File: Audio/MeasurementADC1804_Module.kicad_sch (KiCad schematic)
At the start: 78 parts, among them J701 Screw_Terminal_01x02, J702 Screw_Terminal_01x02, J703 Screw_Terminal_01x03, U701 OPA1656, U702 OPA1656, U703 OPA1656, U704 BP5293-50, U705 MBC2596-01, U706 LT1763-3.3, U707 LT1763-5, U708 TPS3808G33DBVR, U709 TPS3808G50DBVR, U710 XC8107AC20MR-G, Y701 ASFL1-12.288MHZ-EC-T

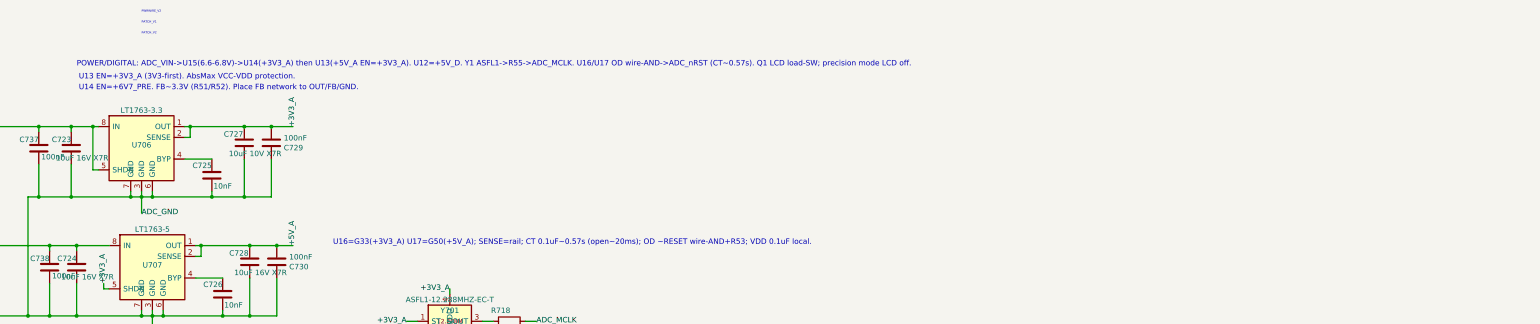
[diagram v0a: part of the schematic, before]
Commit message: レビュー指摘の任意項目を直し、旧注記と未使用AO3401定義を片付ける。
POWER/DIGITAL注記をU704–U710表記に揃え、CT open≈20msに修正。初号はLCD常時ON可と明記する。

Co-authored-by: Cursor <cursoragent@cursor.com>
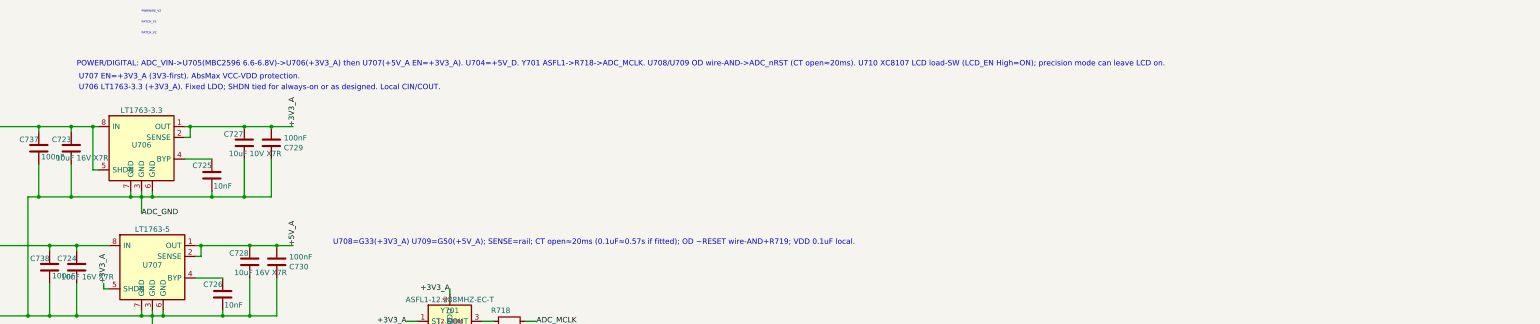
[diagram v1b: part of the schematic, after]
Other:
- note added: "POWER/DIGITAL: ADC_VIN->U705(MBC2596 6.6-6.8V)->U706(+3V3_A) then U707(+5V_A EN=+3V3_A). U704=+5V_D. Y701 ASFL1->R718->ADC_MCLK. U708/U709 OD wire-AND->ADC_nRST (CT open≈20ms). U710 XC8107 LCD load-SW (LCD_EN High=ON); precision mode can leave LCD on."
- note added: "U706 LT1763-3.3 (+3V3_A). Fixed LDO; SHDN tied for always-on or as designed. Local CIN/COUT."
- note added: "U707 EN=+3V3_A (3V3-first). AbsMax VCC-VDD protection."
- note added: "U708=G33(+3V3_A) U709=G50(+5V_A); SENSE=rail; CT open≈20ms (0.1uF≈0.57s if fitted); OD ~RESET wire-AND+R719; VDD 0.1uF local."
- note removed: "POWER/DIGITAL: ADC_VIN->U15(6.6-6.8V)->U14(+3V3_A) then U13(+5V_A EN=+3V3_A). U12=+5V_D. Y1 ASFL1->R55->ADC_MCLK. U16/U17 OD wire-AND->ADC_nRST (CT~0.57s). Q1 LCD load-SW; precision mode LCD off."
- note removed: "U13 EN=+3V3_A (3V3-first). AbsMax VCC-VDD protection."
- note removed: "U14 EN=+6V7_PRE. FB~3.3V (R51/R52). Place FB network to OUT/FB/GND."
- note removed: "U16=G33(+3V3_A) U17=G50(+5V_A); SENSE=rail; CT 0.1uF~0.57s (open~20ms); OD ~RESET wire-AND+R53; VDD 0.1uF local."

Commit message: U710注記を初号LCD常時ON可に合わせて更新する。
Co-authored-by: Cursor <cursoragent@cursor.com>
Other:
- note added: "U710 XC8107AC20MR-G ロードスイッチ: LCD_EN High=ON / Low・Hi-Z=OFF（Active High, VCEH 1.5V min → Pico 3.3V で直接駆動可）。R717 100k=CE プルダウンで起動時 OFF。初号は常時 ON 可。OFF 運用時は SPI/タッチを Low/Hi-Z に。ソフトスタート 0.6ms typ・短絡/逆流/過熱/UVLO 保護内蔵。C740=CIN, C739=CL は各 10uF/3216 を IC 直近へ。FLG は未使用（NC）。"
- note removed: "U710 XC8107AC20MR-G ロードスイッチ: LCD_EN High=ON / Low・Hi-Z=OFF（Active High, VCEH 1.5V min → Pico 3.3V で直接駆動可）。R717 100k=CE プルダウンで起動時 OFF。ノイズ床測定は LCD_EN=Low のまま。ソフトスタート 0.6ms typ・短絡/逆流/過熱/UVLO 保護内蔵。C740=CIN, C739=CL は各 10uF/3216 を IC 直近へ（推奨 1uF 以上）。FLG は未使用（NC）。"
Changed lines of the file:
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@@
 		)
 	)
-	(text "U710 XC8107AC20MR-G ロードスイッチ: LCD_EN High=ON / Low・Hi-Z=OFF（Active High, VCEH 1.5V min → Pico 3.3V で直接駆動可）。R717 100k=CE プルダウンで起動時 OFF。ノイズ床測定は LCD_EN=Low のまま。ソフトスタート 0.6ms typ・短絡/逆流/過熱/UVLO 保護内蔵。C740=CIN, C739=CL は各 10uF/3216 を IC 直近へ（推奨 1uF 以上）。FLG は未使用（NC）。"
+	(text "U710 XC8107AC20MR-G ロードスイッチ: LCD_EN High=ON / Low・Hi-Z=OFF（Active High, VCEH 1.5V min → Pico 3.3V で直接駆動可）。R717 100k=CE プルダウンで起動時 OFF。初号は常時 ON 可。OFF 運用時は SPI/タッチを Low/Hi-Z に。ソフトスタート 0.6ms typ・短絡/逆流/過熱/UVLO 保護内蔵。C740=CIN, C739=CL は各 10uF/3216 を IC 直近へ。FLG は未使用（NC）。"
 		(exclude_from_sim no)
 		(at 312.42 163.83 0)

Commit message: MeasurementADCの配置準備とMBC2596向き修正、KiCad MCP設定を追加する。
C739/C740を購入済み3216に合わせ、ゾーン仮配置とREADMEのポータブルMCP手順を残す。

Co-authored-by: Cursor <cursoragent@cursor.com>
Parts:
- C739: renamed from C733; value 100nF -> 10uF 50V X7R; footprint Capacitor_THT:C_Disc_D5.0mm_W2.5mm_P5.00mm -> Capacitor_SMD:C_1206_3216Metric_Pad1.33x1.80mm_HandSolder
- C740: renamed from C734; value 100nF -> 10uF 50V X7R; footprint Capacitor_THT:C_Disc_D5.0mm_W2.5mm_P5.00mm -> Capacitor_SMD:C_1206_3216Metric_Pad1.33x1.80mm_HandSolder
- J701: value Screw_Terminal_01x02 -> AUDIO
- J702: value Screw_Terminal_01x02 -> V_IN
- J703: value Screw_Terminal_01x03 -> 15_V_IN
- renumbered C712 to C711, C713 to C712, C717 to C713, C718 to C714, C719 to C715, C720 to C716, C721 to C717, C722 to C718, C711 to C719, C715 to C720, C714 to C721, C716 to C722, C740 to C723, C737 to C724, C738 to C725, C723 to C726, C724 to C727, C736 to C728, C735 to C729, C725 to C730, C726 to C731, C727 to C732, C728 to C733, C739 to C734, C729 to C735, C730 to C736, C731 to C737, C732 to C738, U710 to U708, U708 to U709, U709 to U710

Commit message: ムラタRDEのフットプリントを実寸に合わせ、STATUSを現状に更新する。
Disc φ5汎用FPが過大で干渉誤認の原因だったため、発注品RDER71Hに合わせたFPへ20箇所を差し替える。

Co-authored-by: Cursor <cursoragent@cursor.com>
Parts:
- C701, C702, C705, C706, C711, C712, C717, C718, C719, C720, C722, C724, C725, C728, C730, C731, C735, C736, C737, C738: footprint Capacitor_THT:C_Disc_D5.0mm_W2.5mm_P5.00mm -> Library:C_Murata_RDE_L4.0mm_W3.5mm_T2.5mm_P5.00mm
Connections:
- net +15V_A: now also J703.3 (Pin_3); no longer J703.1 (Pin_1)
- net -15V_A: now also J703.1 (Pin_1); no longer J703.3 (Pin_3)
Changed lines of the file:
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@@
 		)
 	)
+	(label "-15V_A"
+		(at 111.76 227.33 0)
+		(effects
+			(font
+				(size 1.27 1.27)
+			)
+			(justify left bottom)
+		)
+	)
 	(label "AUDIO_L_IN"
 		(at 33.02 26.67 180)
@@
 		)
 	)
-	(label "-15V_A"
-		(at 101.6 227.33 180)
+	(label "TP_SDA"
+		(at 247.65 177.8 180)
 		(effects
 			(font
 				(size 1.27 1.27)
 			)
-			(justify right bottom)
+			(justify right)
 		)
 	)
-	(label "TP_SDA"
-		(at 247.65 177.8 180)
+	(label "+15V_A"
+		(at 101.6 227.33 180)
 		(effects
 			(font
 				(size 1.27 1.27)
 			)
-			(justify right)
+			(justify right bottom)
 		)
 	)
@@
 		)
 	)
-	(label "+15V_A"
-		(at 111.76 227.33 0)
-		(effects
-			(font
-				(size 1.27 1.27)
-			)
-			(justify left bottom)
-		)
-	)
 	(label "LCD_CS"
 		(at 194.31 171.45 180)
@@
 		)
 	)
-	(hierarchical_label "-15V_A"
-		(shape input)
-		(at 102.87 223.52 180)
+	(hierarchical_label "A_GND"
+		(shape bidirectional)
+		(at 105.41 215.9 180)
 		(effects
 			(font
@@
 		)
 	)
-	(hierarchical_label "A_GND"
-		(shape bidirectional)
-		(at 105.41 215.9 180)
+	(hierarchical_label "ADC_GND_IN"
+		(shape input)
+		(at 66.04 219.71 0)
 		(effects
 			(font
 				(size 1.524 1.524)
 			)
-			(justify right)
+			(justify left)
 		)
 	)
-	(hierarchical_label "+15V_A"
+	(hierarchical_label "ADC_V_IN"
 		(shape input)
-		(at 110.49 223.52 0)
+		(at 63.5 219.71 180)
 		(effects
 			(font
 				(size 1.524 1.524)
 			)
-			(justify left)
+			(justify right)
 		)
 	)
-	(hierarchical_label "ADC_GND_IN"
+	(hierarchical_label "-15V_A"
 		(shape input)
-		(at 66.04 219.71 0)
+		(at 110.49 223.52 0)
 		(effects
 			(font
@@
 		)
 	)
-	(hierarchical_label "ADC_V_IN"
+	(hierarchical_label "AUDIO_R_IN"
 		(shape input)
-		(at 63.5 219.71 180)
+		(at 22.86 219.71 180)
 		(effects
 			(font
@@
 		)
 	)
-	(hierarchical_label "AUDIO_R_IN"
+	(hierarchical_label "+15V_A"
 		(shape input)
-		(at 22.86 219.71 180)
+		(at 102.87 223.52 180)
 		(effects
 			(font
@@
 			)
 		)
-		(property "Footprint" "Capacitor_THT:C_Disc_D5.0mm_W2.5mm_P5.00mm"
+		(property "Footprint" "Library:C_Murata_RDE_L4.0mm_W3.5mm_T2.5mm_P5.00mm"
 			(at 34.29 196.85 0)
 			(hide yes)
@@
 			)
 		)
-		(property "Footprint" "Capacitor_THT:C_Disc_D5.0mm_W2.5mm_P5.00mm"
+		(property "Footprint" "Library:C_Murata_RDE_L4.0mm_W3.5mm_T2.5mm_P5.00mm"
 			(at 316.23 36.83 0)
 			(hide yes)
@@
 			)
 		)
-		(property "Footprint" "Capacitor_THT:C_Disc_D5.0mm_W2.5mm_P5.00mm"
+		(property "Footprint" "Library:C_Murata_RDE_L4.0mm_W3.5mm_T2.5mm_P5.00mm"
 			(at 370.84 35.56 0)
 			(hide yes)
@@
 			)
 		)
-		(property "Footprint" "Capacitor_THT:C_Disc_D5.0mm_W2.5mm_P5.00mm"
+		(property "Footprint" "Library:C_Murata_RDE_L4.0mm_W3.5mm_T2.5mm_P5.00mm"
 			(at 72.39 196.85 0)
 			(hide yes)
@@
 			)
 		)
-		(property "Footprint" "Capacitor_THT:C_Disc_D5.0mm_W2.5mm_P5.00mm"
+		(property "Footprint" "Library:C_Murata_RDE_L4.0mm_W3.5mm_T2.5mm_P5.00mm"
 			(at 359.41 71.12 0)
 			(hide yes)
@@
 			)
 		)
-		(property "Footprint" "Capacitor_THT:C_Disc_D5.0mm_W2.5mm_P5.00mm"
+		(property "Footprint" "Library:C_Murata_RDE_L4.0mm_W3.5mm_T2.5mm_P5.00mm"
 			(at 104.14 196.85 0)
 			(hide yes)
@@
 			)
 		)
-		(property "Footprint" "Capacitor_THT:C_Disc_D5.0mm_W2.5mm_P5.00mm"
+		(property "Footprint" "Library:C_Murata_RDE_L4.0mm_W3.5mm_T2.5mm_P5.00mm"
 			(at 330.2 130.81 0)
 			(hide yes)
@@
 			)
 		)
-		(property "Footprint" "Capacitor_THT:C_Disc_D5.0mm_W2.5mm_P5.00mm"
+		(property "Footprint" "Library:C_Murata_RDE_L4.0mm_W3.5mm_T2.5mm_P5.00mm"
 			(at 398.78 134.62 0)
 			(hide yes)
@@
 			)
 		)
-		(property "Footprint" "Capacitor_THT:C_Disc_D5.0mm_W2.5mm_P5.00mm"
+		(property "Footprint" "Library:C_Murata_RDE_L4.0mm_W3.5mm_T2.5mm_P5.00mm"
 			(at 152.4 41.91 0)
 			(hide yes)
@@
 			)
 		)
-		(property "Footprint" "Capacitor_THT:C_Disc_D5.0mm_W2.5mm_P5.00mm"
+		(property "Footprint" "Library:C_Murata_RDE_L4.0mm_W3.5mm_T2.5mm_P5.00mm"
 			(at 356.87 43.18 0)
 			(hide yes)
@@
 			)
 		)
-		(property "Footprint" "Capacitor_THT:C_Disc_D5.0mm_W2.5mm_P5.00mm"
+		(property "Footprint" "Library:C_Murata_RDE_L4.0mm_W3.5mm_T2.5mm_P5.00mm"
 			(at 152.4 62.23 0)
 			(hide yes)
@@
 			)
 		)
-		(property "Footprint" "Capacitor_THT:C_Disc_D5.0mm_W2.5mm_P5.00mm"
+		(property "Footprint" "Library:C_Murata_RDE_L4.0mm_W3.5mm_T2.5mm_P5.00mm"
 			(at 34.29 189.23 0)
 			(hide yes)
@@
 			)
 		)
-		(property "Footprint" "Capacitor_THT:C_Disc_D5.0mm_W2.5mm_P5.00mm"
+		(property "Footprint" "Library:C_Murata_RDE_L4.0mm_W3.5mm_T2.5mm_P5.00mm"
 			(at 135.89 196.85 0)
 			(hide yes)
@@
 			)
 		)
-		(property "Footprint" "Capacitor_THT:C_Disc_D5.0mm_W2.5mm_P5.00mm"
+		(property "Footprint" "Library:C_Murata_RDE_L4.0mm_W3.5mm_T2.5mm_P5.00mm"
 			(at 104.14 189.23 0)
 			(hide yes)
@@
 			)
 		)
-		(property "Footprint" "Capacitor_THT:C_Disc_D5.0mm_W2.5mm_P5.00mm"
+		(property "Footprint" "Library:C_Murata_RDE_L4.0mm_W3.5mm_T2.5mm_P5.00mm"
 			(at 398.78 104.14 0)
 			(hide yes)
@@
 			)
 		)
-		(property "Footprint" "Capacitor_THT:C_Disc_D5.0mm_W2.5mm_P5.00mm"
+		(property "Footprint" "Library:C_Murata_RDE_L4.0mm_W3.5mm_T2.5mm_P5.00mm"
 			(at 135.89 189.23 0)
 			(hide yes)
@@
 			)
 		)
-		(property "Footprint" "Capacitor_THT:C_Disc_D5.0mm_W2.5mm_P5.00mm"
+		(property "Footprint" "Library:C_Murata_RDE_L4.0mm_W3.5mm_T2.5mm_P5.00mm"
 			(at 372.11 63.5 0)
 			(hide yes)
@@
 			)
 		)
-		(property "Footprint" "Capacitor_THT:C_Disc_D5.0mm_W2.5mm_P5.00mm"
+		(property "Footprint" "Library:C_Murata_RDE_L4.0mm_W3.5mm_T2.5mm_P5.00mm"
 			(at 288.29 46.99 0)
 			(hide yes)
@@
 			)
 		)
-		(property "Footprint" "Capacitor_THT:C_Disc_D5.0mm_W2.5mm_P5.00mm"
+		(property "Footprint" "Library:C_Murata_RDE_L4.0mm_W3.5mm_T2.5mm_P5.00mm"
 			(at 72.39 189.23 0)
 			(hide yes)
@@
 			)
 		)
-		(property "Footprint" "Capacitor_THT:C_Disc_D5.0mm_W2.5mm_P5.00mm"
+		(property "Footprint" "Library:C_Murata_RDE_L4.0mm_W3.5mm_T2.5mm_P5.00mm"
 			(at 318.77 64.77 0)
 			(hide yes)

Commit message: 電源島の配置配線を進め、STATUSに次タスクを残す。
CIN(C741/C742)と+5V_D幹線・U705寄せ・NT702周りを反映し、引き継ぎ用の優先作業を STATUS 先頭にメモした。

Co-authored-by: Cursor <cursoragent@cursor.com>
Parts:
- added C741: 47uF 35V, Capacitor_THT:CP_Radial_D8.0mm_P3.50mm, symbol Device:C_Polarized
- added C742: 100nF, Library:C_Murata_RDE_L4.0mm_W3.5mm_T2.5mm_P5.00mm, symbol Device:C
- added F701: Fuse, symbol Device:Fuse
- A702: footprint Module:RaspberryPi_Pico_Common_Unspecified -> Module:RaspberryPi_Pico_Common_THT
- C705, C706, C711, C712, C717, C718: footprint Library:C_Murata_RDE_L4.0mm_W3.5mm_T2.5mm_P5.00mm -> Capacitor_SMD:C_1206_3216Metric_Pad1.33x1.80mm_HandSolder
- NT701, NT702: footprint NetTie:NetTie-2_THT_Pad1.0mm -> NetTie:NetTie-2_SMD_Pad2.0mm
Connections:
- net ADC_GND_IN: now also J702.2 (Pin_2), C741.2, C742.2; no longer J702.1 (Pin_1)
- net ADC_V_IN: now also C741.1, C742.1, F701.2; no longer J702.2 (Pin_2)
- net AUDIO_L_IN: now also C708.2, J701.2 (Pin_2), R701.2; no longer C710.2, J701.1 (Pin_1), R702.2
- net AUDIO_R_IN: now also C710.2, J701.1 (Pin_1), R702.2; no longer C708.2, J701.2 (Pin_2), R701.2
- net VCOML: now also C720.2, U703.3 (INA+), U703.5 (INB+); no longer C719.2, U702.3 (INA+), U702.5 (INB+)
- net VCOMR: now also C719.2, U702.3 (INA+), U702.5 (INB+); no longer C720.2, U703.3 (INA+), U703.5 (INB+)
- net VINL+: now also R716.1; no longer R714.1
- net VINL-: now also R715.1; no longer R713.1
- net VINR+: now also R714.1; no longer R716.1
- net VINR-: now also R713.1; no longer R715.1
- new net: F701.1, J702.1 (Pin_1)
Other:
- note added: "左チャンネル"
- note added: "階層ポート / 右チャンネル"
- note removed: "右チャンネル"
- note removed: "階層ポート / 左チャンネル"

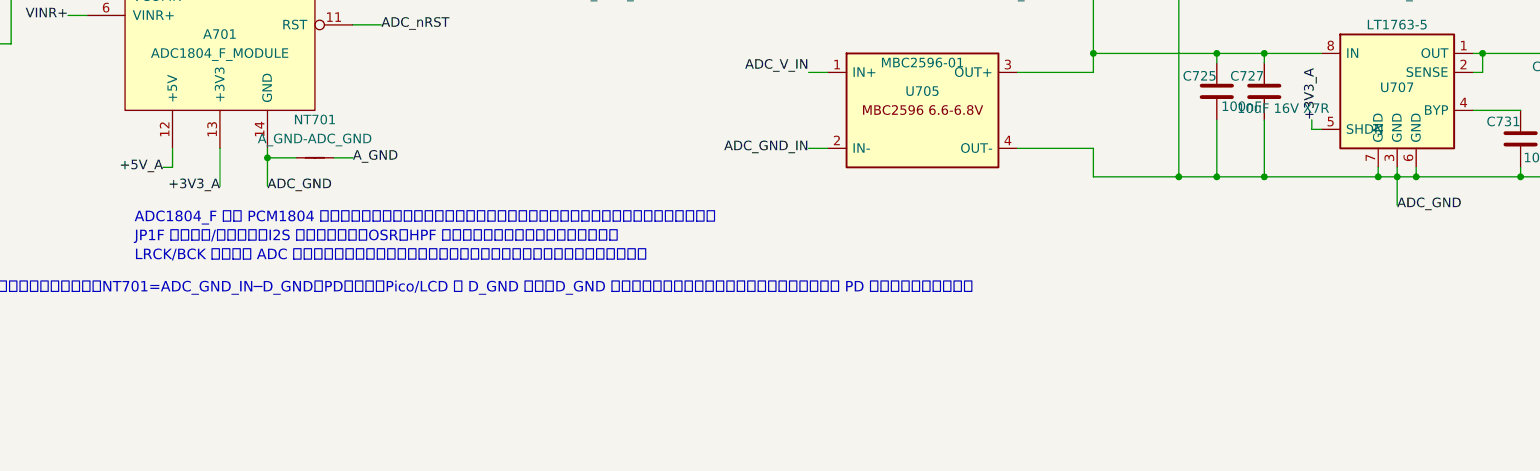
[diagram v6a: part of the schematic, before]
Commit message: 計測ADC周りのDRC・方針整理とGNDベタ直角化を反映する。
A702嵩上げコートヤード緩和、A701固定穴ノッチ、F701/FMT注記、LCDソフト制御とSTATUS更新をまとめる。

Co-authored-by: Cursor <cursoragent@cursor.com>
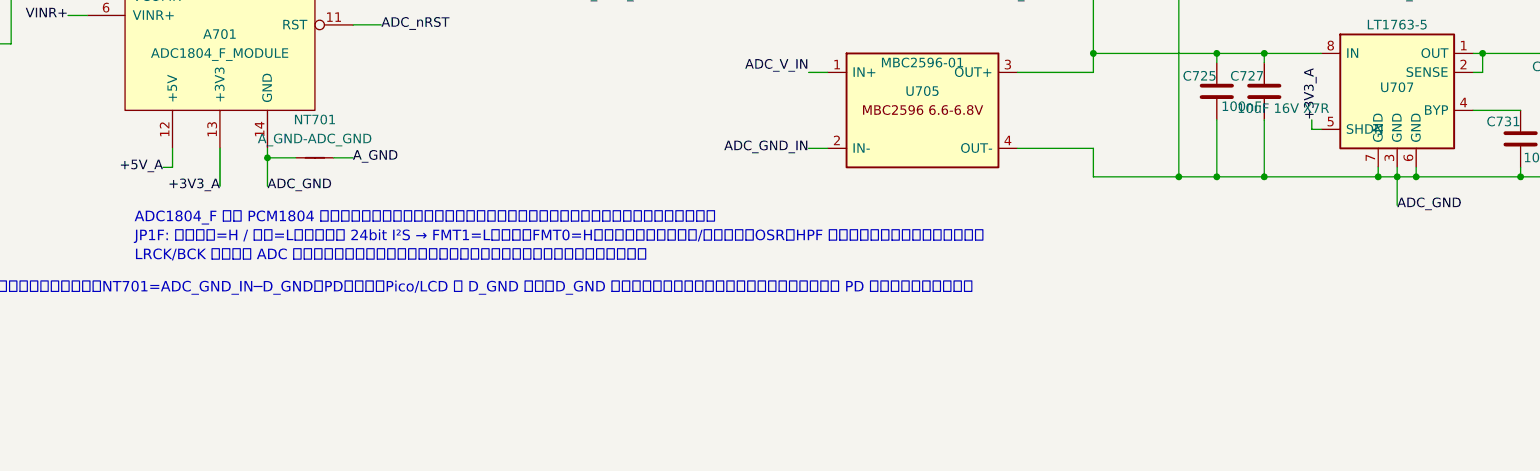
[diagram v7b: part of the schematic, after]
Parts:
- F701: footprint (none) -> Resistor_THT:R_Axial_DIN0411_L9.9mm_D3.6mm_P12.70mm_Horizontal
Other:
- note added: "JP1F: ショート=H / 開放=L。本設計は 24bit I²S → FMT1=L（開放）FMT0=H（ショート）。マスタ/スレーブ・OSR・HPF はモジュールマニュアルに従う。"
- note removed: "JP1F でマスタ/スレーブ、I2S フォーマット、OSR、HPF をモジュールマニュアルに従い設定。"
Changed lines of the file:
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@@
 		)
 	)
-	(text "JP1F でマスタ/スレーブ、I2S フォーマット、OSR、HPF をモジュールマニュアルに従い設定。"
+	(text "JP1F: ショート=H / 開放=L。本設計は 24bit I²S → FMT1=L（開放）FMT0=H（ショート）。マスタ/スレーブ・OSR・HPF はモジュールマニュアルに従う。"
 		(exclude_from_sim no)
 		(at 173.99 85.09 0)
@@
 			)
 		)
-		(property "Footprint" ""
+		(property "Footprint" "Resistor_THT:R_Axial_DIN0411_L9.9mm_D3.6mm_P12.70mm_Horizontal"
 			(at 67.818 223.52 90)
 			(hide yes)

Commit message: 計測ADC回路図を rev 0.4 として固定し、監視ICを TPS3307 に置き換える。
初号の応急配線（LCD SPI0、D701、GP15=~MR）を正規化し、U709 VDD 短絡も直した。ネット照合用スクリプトも残す。

Co-authored-by: Cursor <cursoragent@cursor.com>
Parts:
- removed C739: 10uF 50V X7R, Capacitor_SMD:C_1206_3216Metric_Pad1.33x1.80mm_HandSolder, symbol Device:C
- removed U709: TPS3808G33DBVR, Package_TO_SOT_SMD:SOT-23-6, symbol MeasurementADC_Extras:TPS3808G33DBVR
- removed U710: TPS3808G50DBVR, Package_TO_SOT_SMD:SOT-23-6, symbol MeasurementADC_Extras:TPS3808G50DBVR
- added C743: 100nF, Capacitor_SMD:C_0603_1608Metric, symbol Device:C
- added C744: 10nF, Capacitor_SMD:C_0603_1608Metric, symbol Device:C
- added D701: RB160M-30, Diode_SMD:D_SOD-123, symbol Device:D_Schottky
- added R720: 1k, Resistor_SMD:R_1206_3216Metric_Pad1.30x1.75mm_HandSolder, symbol Device:R
- added TP701: ADC_MCLK, TestPoint:TestPoint_Pad_D1.5mm, symbol Connector:TestPoint
- added U709: TPS3307-33D, Package_SO:SOIC-8_3.9x4.9mm_P1.27mm, symbol MeasurementADC_Extras:TPS3307-33
- C737: value 10nF -> 100nF; footprint Library:C_Murata_RDE_L4.0mm_W3.5mm_T2.5mm_P5.00mm -> Capacitor_SMD:C_0603_1608Metric
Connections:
- net +3V3_A: now also C743.1, C744.1, U709.2 (SENSE2), U709.3 (SENSE3), U709.8 (VDD); no longer C737.2
- net +5V_A: now also C737.2, U709.1 (SENSE1)
- net +5V_D: now also D701.2 (A); no longer A702.39 (VSYS)
- net ADC_GND: now also C743.2, C744.2, U709.4 (GND)
- net ADC_MCLK: now also R720.1, TP701.1
- net ADC_nRST: now also U709.5 (~{RESET})
- net LCD_MOSI: now also A702.25 (GPIO19); no longer A702.6 (GPIO4)
- net LCD_SCK: now also A702.24 (GPIO18); no longer A702.5 (GPIO3)
- net MCLK_SENSE: now reaches A702.12 (GPIO9)
- net MCLK_SENSE: now also R720.2
- net ADC_nMR: now reaches A702.20 (GPIO15)
- net ADC_nMR: now also U709.7 (~{MR})
- new net VSYS: A702.39 (VSYS), D701.1 (K)
- no-connect marks 22 -> 18
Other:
- note added: "A3 Pico2 横置き: 南列 1-20 西→東 / 北列 21-40 東→西。VSYS=+5V_D via D701 ショットキ, GND=D_GND | GP0=ADC_DATA GP1=ADC_BCK GP2=ADC_LRCK | GP3/GP4=NC(旧 LCD SPI) | GP5=LCD_CS GP6=LCD_DC GP7=LCD_RST GP8=LCD_EN | GP9=MCLK_SENSE (R720 1k, 入力専用) | GP10=TP_SDA GP11=TP_SCL GP12=TP_INT GP13=TP_RST | GP15=ADC_nMR (TPS3307 ~MR, OD, H は駆動しない) | GP18=LCD_SCK GP19=LCD_MOSI (SPI0)"
- note added: "GP15=ADC_nMR は TPS3307 の ~MR。オープンドレインのみ、H は駆動しない。 ~RESET はプッシュプルなので ADC_nRST には直接ワイヤ AND しない。"
- note added: "GP9=MCLK_SENSE は R720 1k 経由の入力専用。出力にすると Y701 と衝突して SCKI が化ける。"
- note added: "JP1F: ショート=H / 開放=L。本設計は S/M=L, OSR2=L OSR1=H OSR0=H（ADCマスタ 48k/256fs）、24bit I²S → FMT1=L（開放）FMT0=H（ショート）。HPF はモジュールマニュアルに従う。"
- note added: "POWER/DIGITAL: ADC_VIN->U705(MBC2596 6.6-6.8V)->U706(+3V3_A) then U707(+5V_A EN=+3V3_A). U704=+5V_D; D701 Schottky +5V_D->VSYS so USB cannot backfeed +5V_D. Y701 ASFL1->R718->ADC_MCLK (TP701; R720 1k to GP9 sense). U709 TPS3307-33D SO-8 watches +5V_A/+3V3_A, ~RESET->ADC_nRST (PP, 200ms), GP15 OD -> ~MR. U708 XC8107 LCD load-SW (LCD_EN High=ON)."
- note added: "U708 XC8107AC20MR-G ロードスイッチ: LCD_EN High=ON / Low・Hi-Z=OFF（Active High, VCEH 1.5V min → Pico 3.3V で直接駆動可）。R717 100k=CE プルダウンで起動時 OFF。初号は常時 ON 可。OFF 運用時は SPI/タッチを Low/Hi-Z に。ソフトスタート 0.6ms typ・短絡/逆流/過熱/UVLO 保護内蔵。C740=CIN, C739=CL は各 10uF/3216 を IC 直近へ。FLG は未使用（NC）。"
- note added: "U709=TPS3307-33D SO-8: SENSE1=+5V_A (4.55V) SENSE2=+3V3_A (2.93V) SENSE3=VDD; VDD=+3V3_A C745 100nF; ~RESET PP -> ADC_nRST + R719; GP15 OD -> ~MR (do not drive H); RESET pin NC; 200ms delay. Replaces TPS3808G33/G50 SOT-23-6."
- note added: "電源: USB VBUS → Pico 内部ショットキ → VSYS。D701 が +5V_D への逆流を止めるので、USB だけ挿すと Pico は動き LCD は消える。VBUS(pin40) は NC。"
- note removed: "A3 Pico2: VSYS=+5V_D GND=D_GND | GP0=ADC_DATA GP1=ADC_BCK GP2=ADC_LRCK | GP3=LCD_SCK GP4=LCD_MOSI GP5=LCD_CS GP6=LCD_DC GP7=LCD_RST GP8=LCD_EN | GP10=TP_SDA GP11=TP_SCL GP12=TP_INT GP13=TP_RST. Wire labels to pins in EESchema."
- note removed: "JP1F: ショート=H / 開放=L。本設計は 24bit I²S → FMT1=L（開放）FMT0=H（ショート）。マスタ/スレーブ・OSR・HPF はモジュールマニュアルに従う。"
- note removed: "POWER/DIGITAL: ADC_VIN->U705(MBC2596 6.6-6.8V)->U706(+3V3_A) then U707(+5V_A EN=+3V3_A). U704=+5V_D. Y701 ASFL1->R718->ADC_MCLK. U708/U709 OD wire-AND->ADC_nRST (CT open≈20ms). U710 XC8107 LCD load-SW (LCD_EN High=ON); precision mode can leave LCD on."
- note removed: "U708=G33(+3V3_A) U709=G50(+5V_A); SENSE=rail; CT open≈20ms (0.1uF≈0.57s if fitted); OD ~RESET wire-AND+R719; VDD 0.1uF local."
- note removed: "U710 XC8107AC20MR-G ロードスイッチ: LCD_EN High=ON / Low・Hi-Z=OFF（Active High, VCEH 1.5V min → Pico 3.3V で直接駆動可）。R717 100k=CE プルダウンで起動時 OFF。初号は常時 ON 可。OFF 運用時は SPI/タッチを Low/Hi-Z に。ソフトスタート 0.6ms typ・短絡/逆流/過熱/UVLO 保護内蔵。C740=CIN, C739=CL は各 10uF/3216 を IC 直近へ。FLG は未使用（NC）。"
- moved on the sheet: C738, R718, R719, Y701
